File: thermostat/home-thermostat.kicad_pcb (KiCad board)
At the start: 4 copper layers, 142.5 x 50.2 mm, 136 parts, among them J1 Amphenol_132289 SMA, J2 Conn_01x24, J3 Thermosthat, J4 Conn_ARM_JTAG_SWD_10, J5 Conn_01x20, J6 Conn_02x02_Odd_Even, J7 Thermosthat, Q1 BSS806NL6327, Q2 BC817, Q3 BC817, Q4 BC817, Q5 BC817, Q6 BC817, U1 MKW41Z512VHT, U10 SN74LVC2T45DCUR, U2 MCP7940N-xMS, U3 MCP9844, U4 AT24C512, U5 LM2574M-5, U6 LD1117S33TR_SOT223, U7 LM358, U8 PCF8574, U9 SN74LVC2T45DCUR, Y1 32MHz 10PPM SMT 2.0x1.6mm 10PF, Y2 32.768KHz 20PPM 3.2x1.5mm 7PF, Y3 32.768KHz 20PPM 3.2x1.5mm 7PF

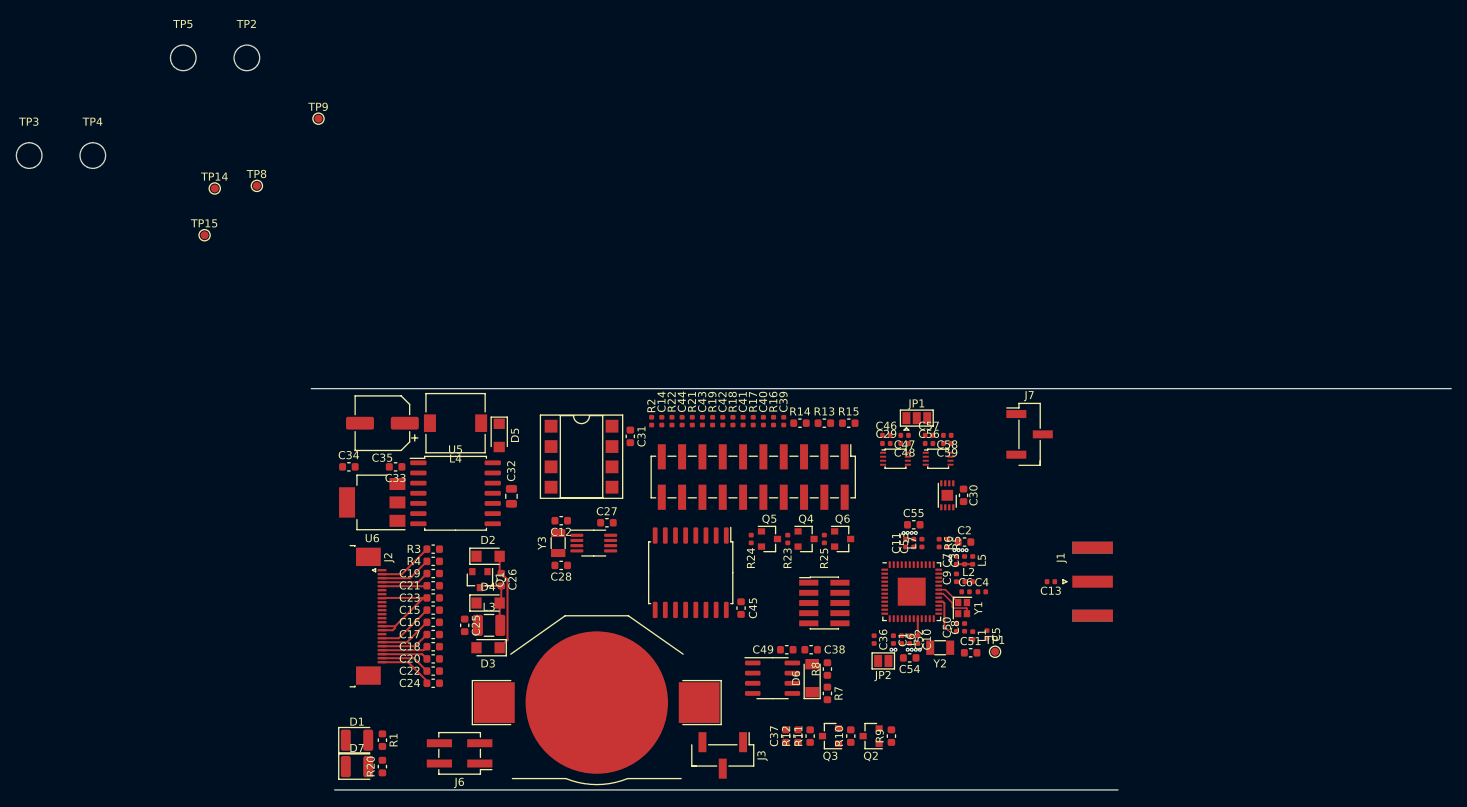
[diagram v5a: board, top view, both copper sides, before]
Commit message: Changed LED and regulator_out drivers to NMOS instead of bipolar. Started routing, SPI and I2C lines done.
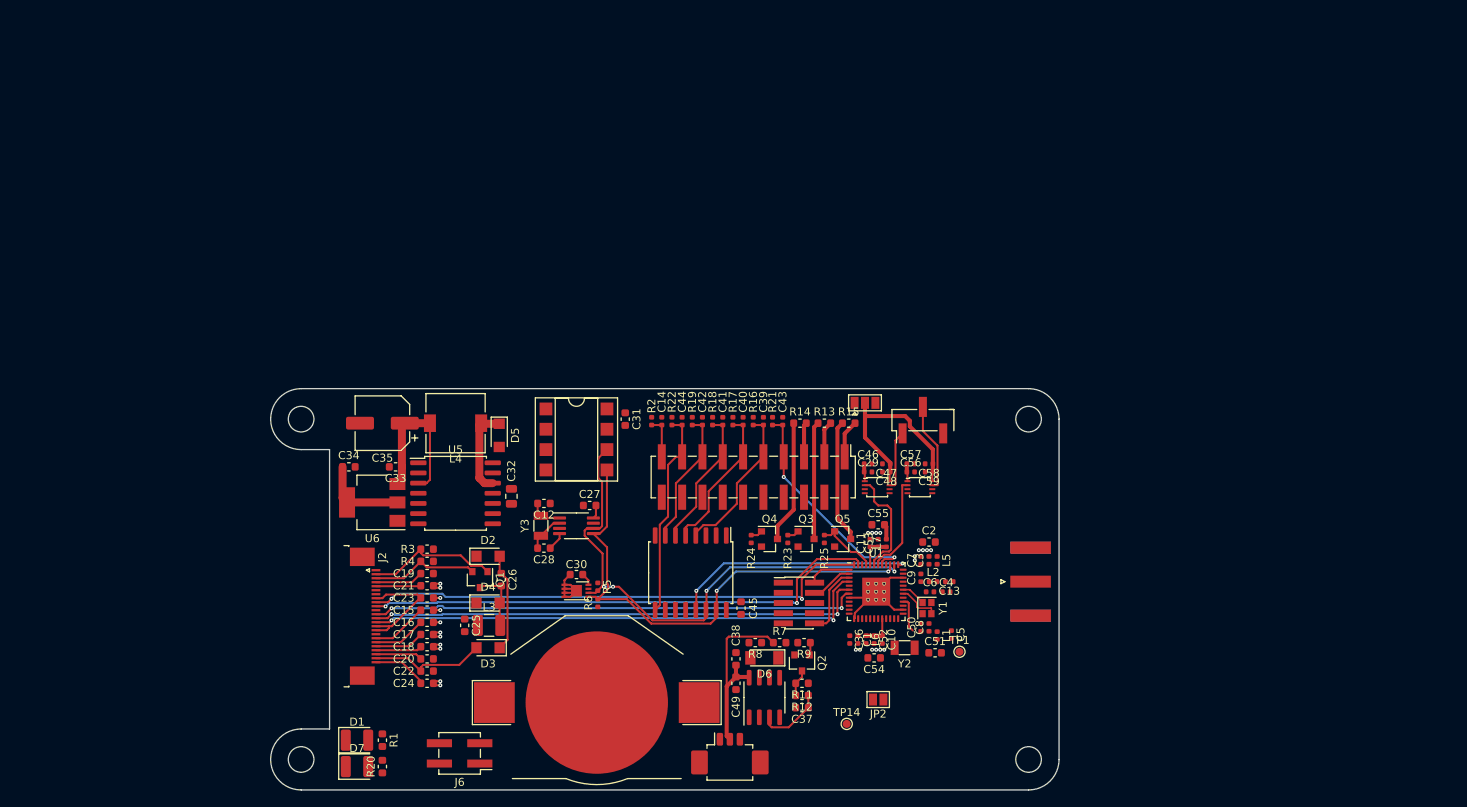
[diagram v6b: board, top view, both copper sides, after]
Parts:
- removed Q6: BC817, Package_TO_SOT_SMD:SOT-23
- removed R10: 4K7?, Resistor_SMD:R_0603_1608Metric
- removed TP15: 5V, TestPoint:TestPoint_Pad_D1.0mm
- removed TP8: 3V3, TestPoint:TestPoint_Pad_D1.0mm
- removed TP9: GND, TestPoint:TestPoint_Pad_D1.0mm
- J3: value Thermosthat -> Thermosthat - Molex PicoBlade; footprint Connector_PinHeader_2.54mm:PinHeader_1x03_P2.54mm_Vertical_SMD_Pin1Left -> Connector_Molex:Molex_PicoBlade_53261-0371_1x03-1MP_P1.25mm_Horizontal
- J7: value Thermosthat -> UART
- Q2, Q3, Q4, Q5: value BC817 -> BSS806NL6327
- U1: footprint Package_DFN_QFN:NXP_LQFN-48-1EP_7x7mm_P0.5mm_EP3.5x3.5mm_16xMask0.45x0.45 -> Package_DFN_QFN:NXP_LQFN-48-1EP_7x7mm_P0.5mm_EP3.5x3.5mm_16xMask0.45x0.45_ThermalVias
- moved TP5 137.3 mm to (168.1, 120.4)
- moved TP2 107.6 mm to (168.1, 77.9)
- moved TP14 103.5 mm to (145.4, 116.0)
- moved TP3 82.8 mm to (77.2, 120.4)
- moved C30 49.4 mm to (111.6, 97.3), turned to 180 degrees
- moved U3 47.9 mm to (111.6, 99.3), turned to 0 degrees
- moved R5 44.0 mm to (114.3, 98.8)
- moved R6 43.3 mm to (114.3, 100.8), turned to 90 degrees
- moved TP4 42.0 mm to (77.2, 77.9)
- moved Q3 24.8 mm to (140.3, 92.8), turned to 0 degrees
- moved R9 16.0 mm to (140.1, 105.8), turned to 180 degrees
- moved J7 13.5 mm to (154.9, 78.0), turned to 90 degrees
- moved C13 12.7 mm to (158.2, 98.2)
- moved Q2 12.6 mm to (139.8, 108.3), turned to 270 degrees
- moved R21 10.0 mm to (136.1, 78.1)
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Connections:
- J5 pad 1: /GPIO/RED -> /GPIO/GREEN
- J5 pad 11: /GPIO/BTN_LEFT -> /GPIO/BTN_DOWN
- J5 pad 13: /GPIO/BTN_RIGHT -> /GPIO/BTN_LEFT
- J5 pad 15: /BTN_OK -> /GPIO/BTN_RIGHT
- J5 pad 3: /GPIO/YELLOW -> /GPIO/RED
- J5 pad 5: /GPIO/GREEN -> /GPIO/YELLOW
- J5 pad 7: /GPIO/BTN_UP -> /BTN_OK
- J5 pad 9: /GPIO/BTN_DOWN -> /GPIO/BTN_UP
- Q2 pad 1: Net-(Q2-Pad1) -> /DAC0_OUT
- Q3 pad 1: Net-(Q2-Pad3) -> /TPM0_CH2
- Q4 pad 1: Net-(Q4-Pad1) -> /TPM0_CH1
- Q5 pad 1: Net-(Q5-Pad1) -> /TPM0_CH3
- R11 pad 2: Net-(Q3-Pad3) -> Net-(Q2-Pad3)
- R12 pad 2: Net-(Q3-Pad3) -> Net-(Q2-Pad3)
- R13 pad 1: Net-(Q4-Pad3) -> Net-(Q3-Pad3)
- R13 pad 2: /GPIO/YELLOW -> /GPIO/RED
- R14 pad 1: Net-(Q5-Pad3) -> Net-(Q4-Pad3)
- R14 pad 2: /GPIO/GREEN -> /GPIO/YELLOW
- R15 pad 1: Net-(Q6-Pad3) -> Net-(Q5-Pad3)
- R15 pad 2: /GPIO/RED -> /GPIO/GREEN
- R23 pad 1: Net-(Q4-Pad1) -> /TPM0_CH2
- R23 pad 2: /TPM0_CH1 -> GND
- R24 pad 1: Net-(Q5-Pad1) -> /TPM0_CH1
- R24 pad 2: /TPM0_CH3 -> GND
- R25 pad 1: Net-(Q6-Pad1) -> /TPM0_CH3
- R25 pad 2: /TPM0_CH2 -> GND
- R9 pad 1: Net-(Q2-Pad1) -> /DAC0_OUT
- R9 pad 2: /DAC0_OUT -> GND
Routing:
- net /I2C1_SCL: track 0.00 -> 66.6 mm, vias 0 -> 4
- net /~DP_RST: track 0.00 -> 65.1 mm, vias 0 -> 2
- net /DP_BUSY: track 0.00 -> 63.8 mm, vias 0 -> 2
- net /SPI1_MOSI: track 0.00 -> 63.7 mm, vias 0 -> 2
- net /I2C1_SDA: track 0.00 -> 63.1 mm, vias 0 -> 2
- net /SPI1_SCK: track 0.00 -> 62.4 mm, vias 0 -> 2
- net /SPI1_PCS0: track 0.00 -> 61.2 mm, vias 0 -> 2
- net GND: track 0.00 -> 39.2 mm, vias 0 -> 11
- net /~BTN_INT: track 0.00 -> 30.2 mm, vias 0 -> 2
- net /BTN_OK: track 0.00 -> 28.0 mm, vias 0 -> 2
- net /GPIO/BTN_CANCEL: track 0.00 -> 26.2 mm
- net Net-(C47-Pad1): track 0.00 -> 25.8 mm
- net +36V: track 0.00 -> 23.8 mm
- net +3V3: track 14.7 -> 35.6 mm
- net +5V: track 0.00 -> 19.8 mm
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- added copper zone on In1.Cu, net GND
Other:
- board size 142.5 x 50.2 mm -> 98.6 x 50.2 mm

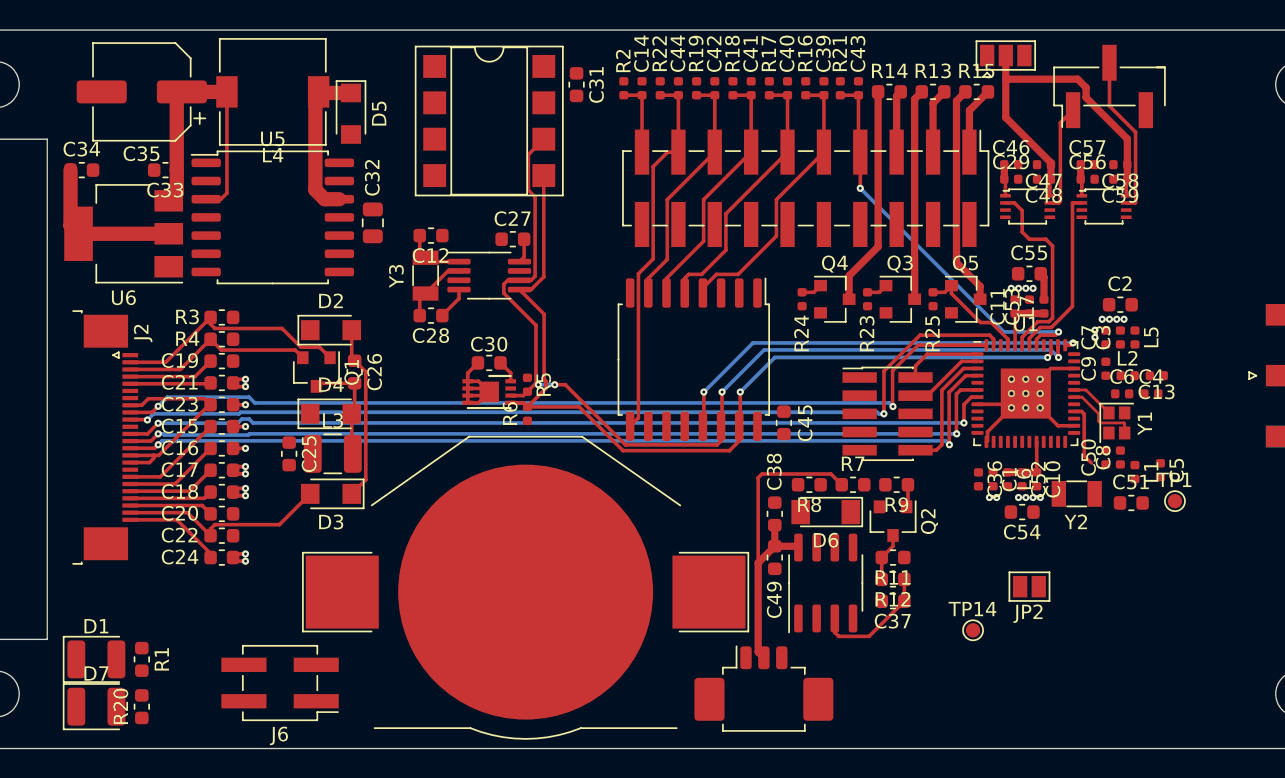
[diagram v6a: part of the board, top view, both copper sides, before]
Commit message: Modivied DRC constraints according to specs of PCB_POOL, finished layouting signal lines, only power is left.
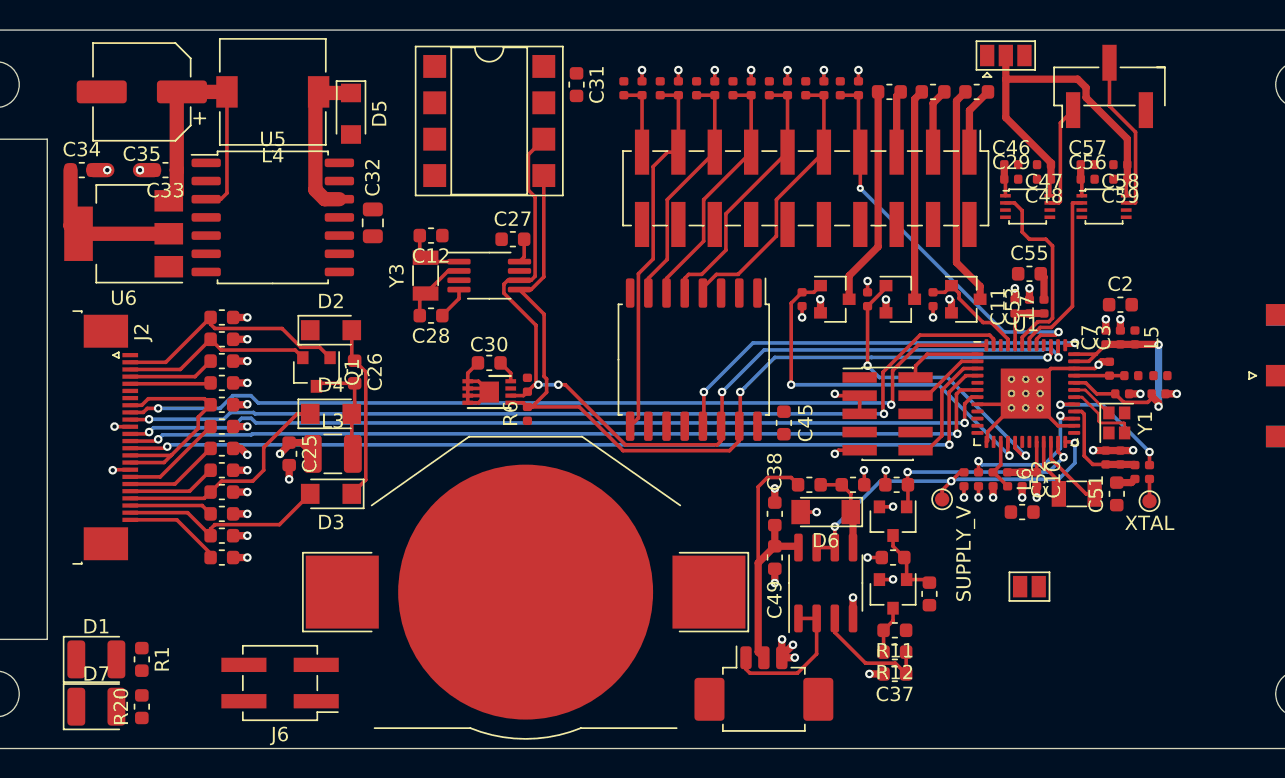
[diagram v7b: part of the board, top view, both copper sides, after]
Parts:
- added C60: 1u, Capacitor_SMD:C_0402_1005Metric, F.Cu at (146.8, 105.4)
- added Q6: BSS806NL6327, Package_TO_SOT_SMD:SOT-23, F.Cu at (139.8, 113.4)
- added R10: 10K, Resistor_SMD:R_0603_1608Metric, F.Cu at (142.4, 113.4)
- added R26: 0, Resistor_SMD:R_0603_1608Metric, F.Cu at (139.8, 110.9)
- TP1: value TestPoint -> XTAL
- moved TP14 9.40 mm to (143.3, 106.8)
- moved C37 5.08 mm to (140.0, 119.0)
- moved R11 5.08 mm to (140.0, 116.0)
- moved R12 5.08 mm to (140.0, 117.5)
- moved R7 3.05 mm to (134.0, 105.8)
- moved R8 3.05 mm to (137.0, 105.8), turned to 0 degrees
- moved TP1 1.78 mm to (157.7, 106.9)
- moved C51 1.20 mm to (155.4, 106.4), turned to 90 degrees
- moved C1 1.02 mm to (145.8, 105.4)
- moved C36 1.02 mm to (144.8, 105.4)
- moved C5 0.77 mm to (157.7, 104.9)
- moved C4 0.51 mm to (158.4, 99.4)
- moved C13 0.25 mm to (158.5, 98.2)
- moved C9 0.25 mm to (154.9, 97.7)
- moved L2 0.25 mm to (156.5, 98.2)
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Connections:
- R11 pad 2: Net-(Q2-Pad3) -> Net-(Q6-Pad3)
- R12 pad 2: Net-(Q2-Pad3) -> Net-(Q6-Pad3)
- U1 pad 15: /VDD_RF -> +3V3
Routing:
- net GND: track 39.2 -> 89.9 mm, vias 11 -> 59
- net /ADC_IN: track 0.00 -> 26.1 mm, vias 0 -> 3
- net /TPM0_CH1: track 1.48 -> 26.5 mm, vias 0 -> 2
- net /VDD_RF: track 0.00 -> 19.7 mm, vias 0 -> 2
- net /TPM0_CH2: track 1.48 -> 21.2 mm, vias 0 -> 2
- net /DAC0_OUT: track 1.58 -> 15.0 mm, vias 0 -> 2
- net /VREF: track 0.00 -> 10.4 mm, vias 0 -> 2
- net /regulator_out/pwm_out: track 0.00 -> 10.2 mm
- net /display/PREVGH: track 5.79 -> 15.9 mm
- net +3V3: track 35.6 -> 45.4 mm, vias 0 -> 1
- net /XTAL_O: track 0.00 -> 9.48 mm, vias 0 -> 2
- net Net-(D6-Pad1): track 0.00 -> 6.18 mm
- net Net-(U1-Pad22): track 0.00 -> 5.25 mm
- net Net-(U1-Pad21): track 0.00 -> 4.07 mm
- net +36V: track 23.8 -> 20.2 mm
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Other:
- net class Default: via_dia 0.5 -> 0.6; via_drill 0.2 -> 0.3
- rule via_min_size: 0.5 -> 0.6
- board text added: "Reference boards have continuous GND layer beneath crystal without gnd slicing"

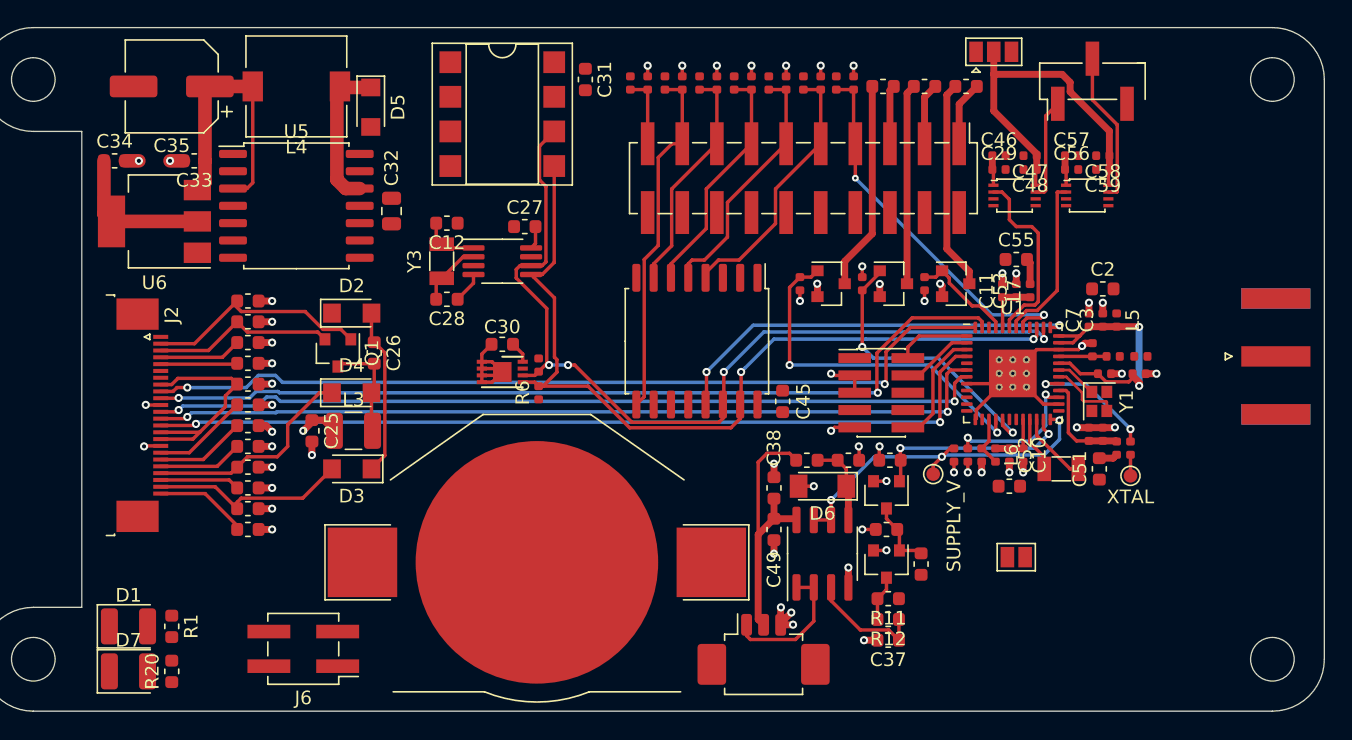
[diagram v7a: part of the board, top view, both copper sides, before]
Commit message: Finished routing except for the RF line, still need to add many many grounding vias.
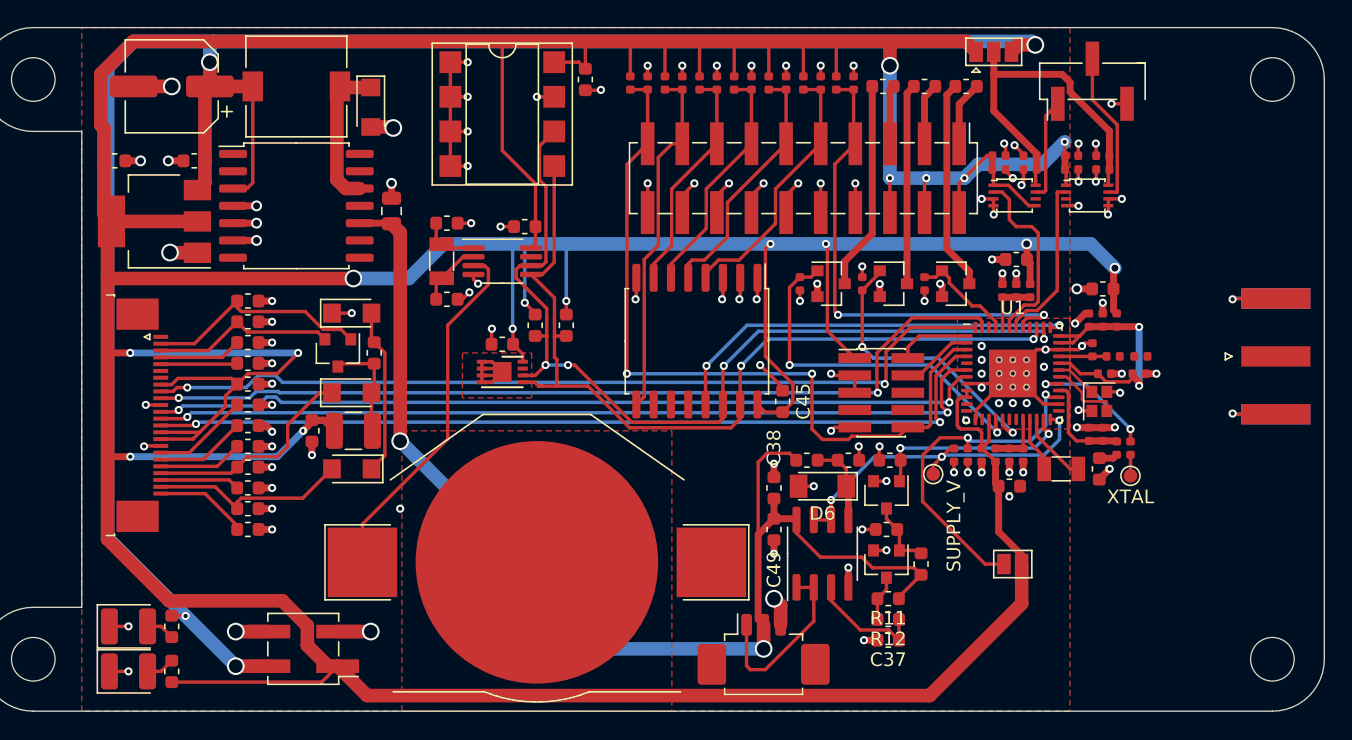
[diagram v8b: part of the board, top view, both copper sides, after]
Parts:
- R5, R6: footprint Resistor_SMD:R_0402_1005Metric -> Resistor_SMD:R_0603_1608Metric
- moved R6 5.35 mm to (116.3, 95.9), turned to 270 degrees
- moved R5 2.93 mm to (114.0, 95.9)
- moved JP2 0.57 mm to (149.1, 113.4)
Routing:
- net +3V3: track 45.4 -> 480.8 mm, vias 1 -> 17
- net +5V: track 19.8 -> 145.4 mm, vias 0 -> 4
- net GND: track 89.9 -> 185.0 mm, vias 59 -> 125
- net +36V: track 20.2 -> 87.3 mm, vias 0 -> 2
- net /RESET_b: track 13.8 -> 57.0 mm, vias 0 -> 2
- net Net-(BT1-Pad1): track 0.00 -> 26.5 mm
- net /VREF: track 10.4 -> 25.6 mm
- net /BTN_OK: track 28.0 -> 35.8 mm
- net /regulator_out/pwm_out: track 10.2 -> 13.3 mm
- net Net-(D7-Pad2): track 0.00 -> 2.10 mm
- net Net-(D1-Pad2): track 0.00 -> 2.10 mm
- net /I2C1_SCL: track 66.7 -> 68.1 mm
- net /I2C1_SDA: track 63.3 -> 64.1 mm
- added copper zone on F.Cu, net GND
- added copper zone on In2.Cu, net GND
